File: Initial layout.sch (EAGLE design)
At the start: 50 parts, among them U2 TPS54540DDARQ1

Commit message: Finished Schematic
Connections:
- new net SPARE_1: U$1.P12, U$2.33/A14
- new net SPARE_2: U$1.P11, U$2.34/A15
- new net SPARE_3: U$1.P8, U$2.35/A16
- new net SPARE_4: U$1.P7, U$2.36/A17
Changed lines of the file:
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@@
 <label x="205.74" y="-414.02" size="1.778" layer="95"/>
 <pinref part="U$2" gate="G$1" pin="13/SCK"/>
-<wire x1="274.32" y1="-256.54" x2="287.02" y2="-256.54" width="0.1524" layer="91"/>
-<wire x1="287.02" y1="-256.54" x2="287.02" y2="-314.96" width="0.1524" layer="91"/>
-<wire x1="287.02" y1="-314.96" x2="187.96" y2="-314.96" width="0.1524" layer="91"/>
+<wire x1="274.32" y1="-256.54" x2="299.72" y2="-256.54" width="0.1524" layer="91"/>
+<wire x1="299.72" y1="-256.54" x2="299.72" y2="-314.96" width="0.1524" layer="91"/>
+<wire x1="299.72" y1="-314.96" x2="187.96" y2="-314.96" width="0.1524" layer="91"/>
 <wire x1="187.96" y1="-314.96" x2="187.96" y2="-414.02" width="0.1524" layer="91"/>
 </segment>
@@
 </segment>
 </net>
+<net name="SPARE_1" class="0">
+<segment>
+<pinref part="U$2" gate="G$1" pin="33/A14"/>
+<wire x1="274.32" y1="-281.94" x2="292.1" y2="-281.94" width="0.1524" layer="91"/>
+<label x="287.02" y="-281.94" size="1.778" layer="95"/>
+</segment>
+<segment>
+<pinref part="U$1" gate="G$1" pin="P12"/>
+<wire x1="391.16" y1="-248.92" x2="403.86" y2="-248.92" width="0.1524" layer="91"/>
+<label x="398.78" y="-248.92" size="1.778" layer="95"/>
+</segment>
+</net>
+<net name="SPARE_2" class="0">
+<segment>
+<pinref part="U$2" gate="G$1" pin="34/A15"/>
+<wire x1="274.32" y1="-279.4" x2="292.1" y2="-279.4" width="0.1524" layer="91"/>
+<label x="287.02" y="-279.4" size="1.778" layer="95"/>
+</segment>
+<segment>
+<pinref part="U$1" gate="G$1" pin="P11"/>
+<wire x1="391.16" y1="-246.38" x2="403.86" y2="-246.38" width="0.1524" layer="91"/>
+<label x="398.78" y="-246.38" size="1.778" layer="95"/>
+</segment>
+</net>
+<net name="SPARE_3" class="0">
+<segment>
+<pinref part="U$2" gate="G$1" pin="35/A16"/>
+<wire x1="274.32" y1="-276.86" x2="292.1" y2="-276.86" width="0.1524" layer="91"/>
+<label x="287.02" y="-276.86" size="1.778" layer="95"/>
+</segment>
+<segment>
+<pinref part="U$1" gate="G$1" pin="P8"/>
+<wire x1="391.16" y1="-236.22" x2="403.86" y2="-236.22" width="0.1524" layer="91"/>
+<label x="398.78" y="-236.22" size="1.778" layer="95"/>
+</segment>
+</net>
+<net name="SPARE_4" class="0">
+<segment>
+<pinref part="U$2" gate="G$1" pin="36/A17"/>
+<wire x1="274.32" y1="-274.32" x2="292.1" y2="-274.32" width="0.1524" layer="91"/>
+<label x="287.02" y="-274.32" size="1.778" layer="95"/>
+</segment>
+<segment>
+<pinref part="U$1" gate="G$1" pin="P7"/>
+<wire x1="391.16" y1="-233.68" x2="403.86" y2="-233.68" width="0.1524" layer="91"/>
+<label x="398.78" y="-233.68" size="1.778" layer="95"/>
+</segment>
+</net>

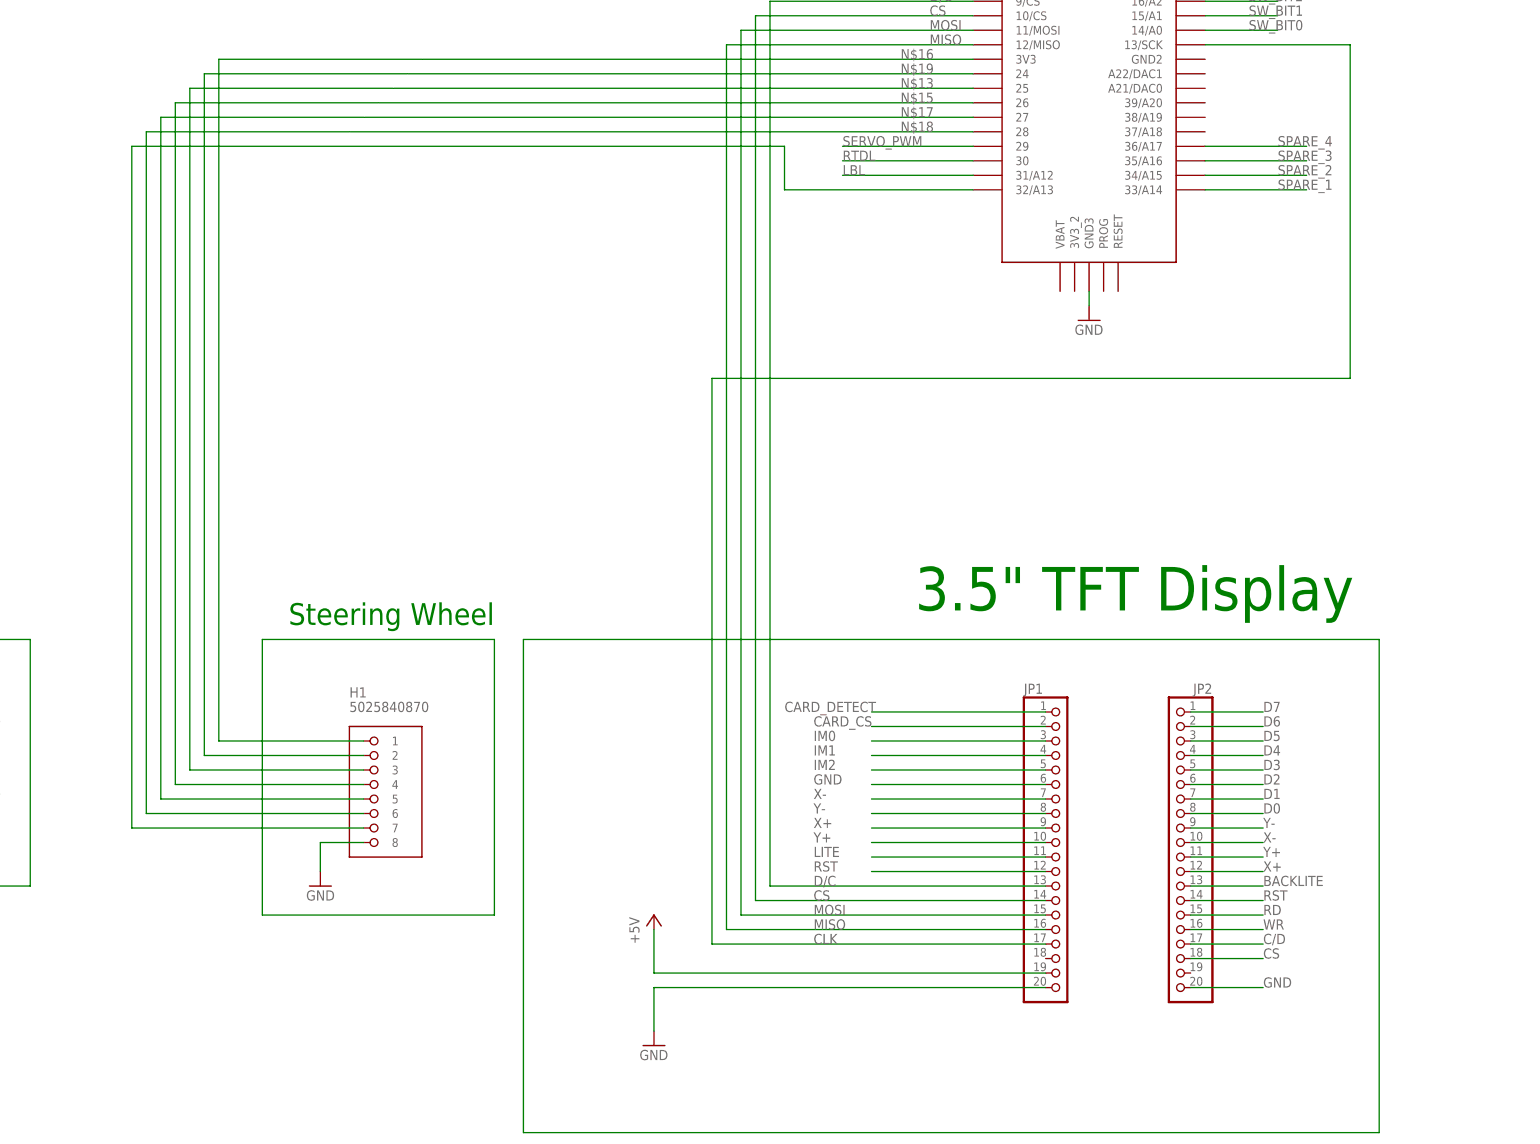
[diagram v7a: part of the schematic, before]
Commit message: Added 4 pin clickmate for rj45
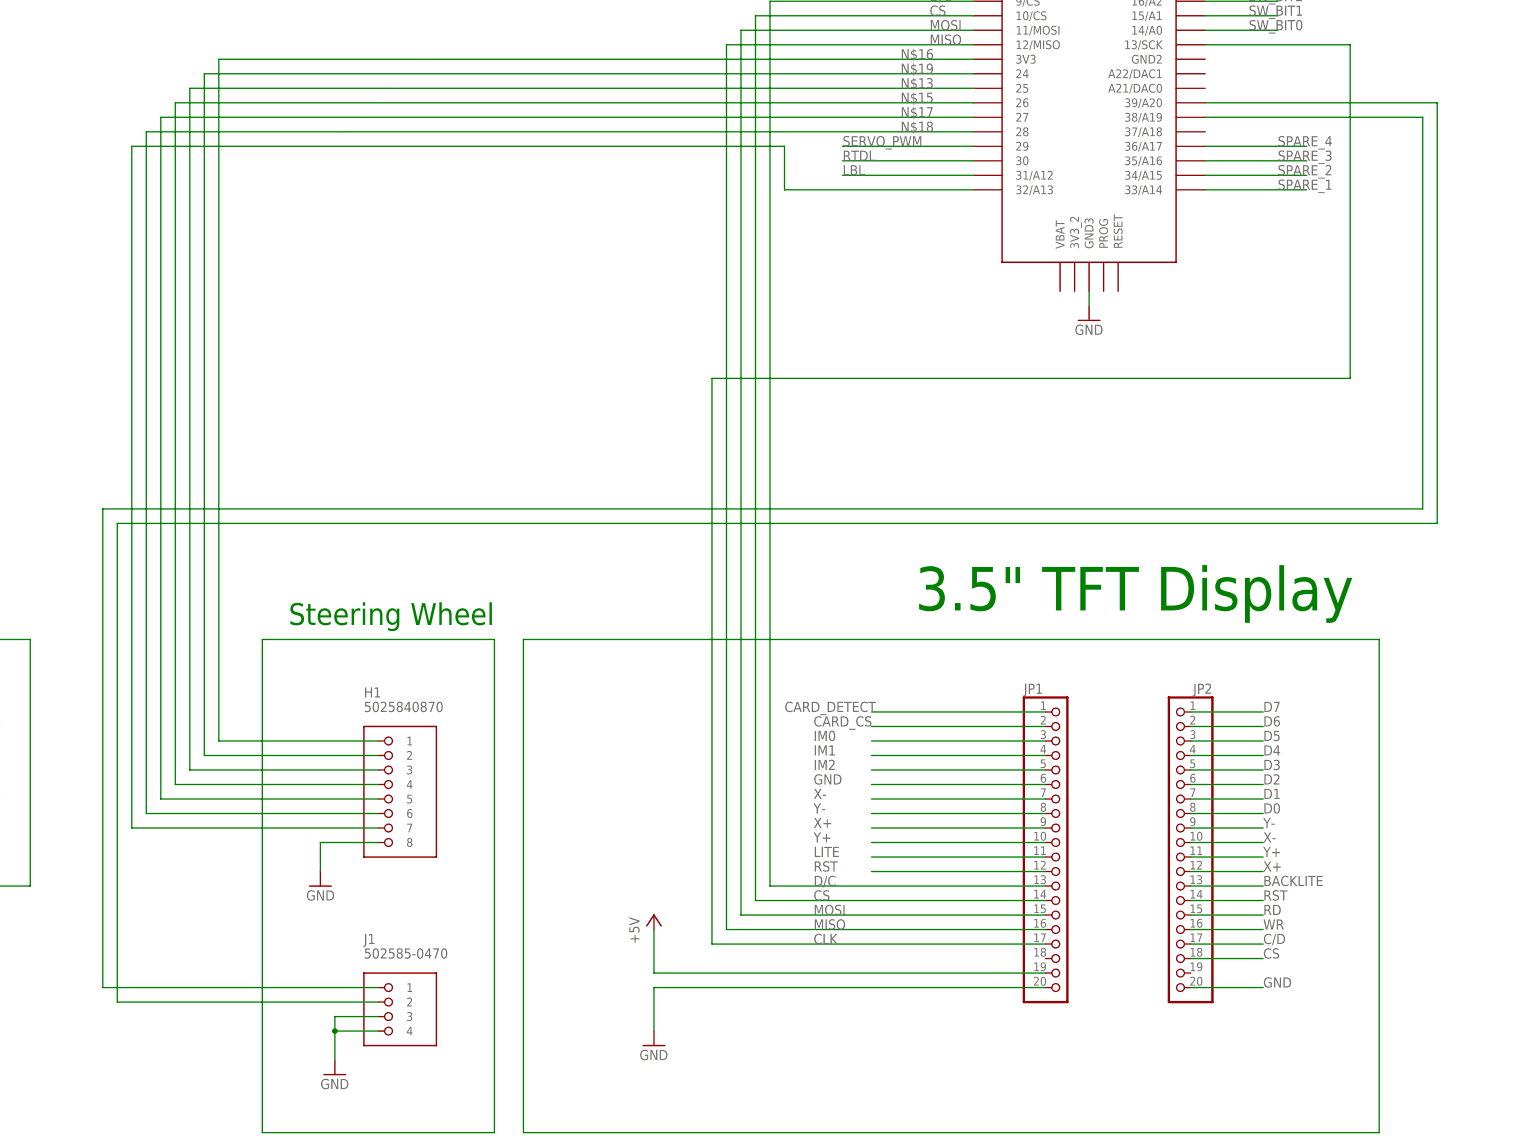
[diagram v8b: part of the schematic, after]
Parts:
- added J1: 502585-0470, FormE:MOLEX_CLICKMATE-4-R/A
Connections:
- new net N$34: J1.1, U$2.38/A19
- new net N$35: J1.2, U$2.39/A20
- net GND: now also J1.3, J1.4
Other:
- moved on the sheet: H1
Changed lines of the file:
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@@
 <layers>
 <layer number="1" name="Top" color="4" fill="1" visible="no" active="no"/>
+<layer number="2" name="GND" color="11" fill="1" visible="no" active="no"/>
+<layer number="3" name="Route3" color="4" fill="3" visible="no" active="no"/>
+<layer number="4" name="Route4" color="1" fill="4" visible="no" active="no"/>
+<layer number="5" name="Route5" color="4" fill="4" visible="no" active="no"/>
+<layer number="6" name="Route6" color="1" fill="8" visible="no" active="no"/>
+<layer number="7" name="Route7" color="4" fill="8" visible="no" active="no"/>
+<layer number="8" name="Route8" color="1" fill="2" visible="no" active="no"/>
+<layer number="9" name="Route9" color="4" fill="2" visible="no" active="no"/>
+<layer number="10" name="Route10" color="1" fill="7" visible="no" active="no"/>
+<layer number="11" name="Route11" color="4" fill="7" visible="no" active="no"/>
+<layer number="12" name="Route12" color="1" fill="5" visible="no" active="no"/>
+<layer number="13" name="Route13" color="4" fill="5" visible="no" active="no"/>
+<layer number="14" name="Route14" color="1" fill="6" visible="no" active="no"/>
+<layer number="15" name="SUPPLY" color="13" fill="1" visible="no" active="no"/>
 <layer number="16" name="Bottom" color="1" fill="1" visible="no" active="no"/>
 <layer number="17" name="Pads" color="2" fill="1" visible="no" active="no"/>
@@
 <part name="GND27" library="supply1" deviceset="GND" device=""/>
 <part name="P+6" library="supply1" deviceset="+5V" device=""/>
+<part name="J1" library="FormE" deviceset="MOLEX_CLICKMATE-4-R/A" device="" value="502585-0470"/>
+<part name="GND23" library="supply1" deviceset="GND" device=""/>
 </parts>
 <sheets>
@@
 <instance part="GND22" gate="1" x="254" y="-304.8"/>
 <instance part="P+7" gate="1" x="431.8" y="-208.28"/>
-<instance part="H1" gate="G$1" x="127" y="-386.08"/>
+<instance part="H1" gate="G$1" x="129.54" y="-386.08"/>
 <instance part="GND24" gate="1" x="119.38" y="-403.86" rot="MR0"/>
 <instance part="U3" gate="G$1" x="30.48" y="-378.46"/>
@@
 <instance part="GND27" gate="1" x="35.56" y="-391.16" rot="R270"/>
 <instance part="P+6" gate="1" x="276.86" y="-198.12"/>
+<instance part="J1" gate="G$1" x="132.08" y="-426.72"/>
+<instance part="GND23" gate="1" x="121.92" y="-436.88"/>
 </instances>
 <busses>
@@
 <segment>
 <pinref part="H1" gate="G$1" pin="8"/>
-<wire x1="127" y1="-396.24" x2="119.38" y2="-396.24" width="0.1524" layer="91"/>
+<wire x1="129.54" y1="-396.24" x2="119.38" y2="-396.24" width="0.1524" layer="91"/>
 <wire x1="119.38" y1="-396.24" x2="119.38" y2="-401.32" width="0.1524" layer="91"/>
 <pinref part="GND24" gate="1" pin="GND"/>
@@
 <wire x1="391.16" y1="-231.14" x2="401.32" y2="-231.14" width="0.1524" layer="91"/>
 <label x="396.24" y="-231.14" size="1.778" layer="95"/>
+</segment>
+<segment>
+<pinref part="J1" gate="G$1" pin="3"/>
+<wire x1="129.54" y1="-426.72" x2="121.92" y2="-426.72" width="0.1524" layer="91"/>
+<pinref part="J1" gate="G$1" pin="4"/>
+<wire x1="121.92" y1="-426.72" x2="121.92" y2="-429.26" width="0.1524" layer="91"/>
+<wire x1="121.92" y1="-429.26" x2="129.54" y2="-429.26" width="0.1524" layer="91"/>
+<wire x1="121.92" y1="-429.26" x2="121.92" y2="-434.34" width="0.1524" layer="91"/>
+<junction x="121.92" y="-429.26"/>
+<pinref part="GND23" gate="1" pin="GND"/>
 </segment>
 </net>
@@
 <pinref part="H1" gate="G$1" pin="7"/>
 <wire x1="86.36" y1="-274.32" x2="200.66" y2="-274.32" width="0.1524" layer="91"/>
-<wire x1="127" y1="-393.7" x2="86.36" y2="-393.7" width="0.1524" layer="91"/>
+<wire x1="129.54" y1="-393.7" x2="86.36" y2="-393.7" width="0.1524" layer="91"/>
 <wire x1="86.36" y1="-393.7" x2="86.36" y2="-274.32" width="0.1524" layer="91"/>
 <pinref part="U$2" gate="G$1" pin="32/A13"/>
@@
 <net name="N$9" class="0">
 <segment>
-<wire x1="149.86" y1="-360.68" x2="149.86" y2="-408.94" width="0.1524" layer="91"/>
-<wire x1="149.86" y1="-408.94" x2="109.22" y2="-408.94" width="0.1524" layer="91"/>
-<wire x1="109.22" y1="-408.94" x2="109.22" y2="-360.68" width="0.1524" layer="91"/>
+<wire x1="149.86" y1="-360.68" x2="149.86" y2="-447.04" width="0.1524" layer="91"/>
+<wire x1="149.86" y1="-447.04" x2="109.22" y2="-447.04" width="0.1524" layer="91"/>
+<wire x1="109.22" y1="-447.04" x2="109.22" y2="-360.68" width="0.1524" layer="91"/>
 <wire x1="109.22" y1="-360.68" x2="149.86" y2="-360.68" width="0.1524" layer="91"/>
 </segment>
@@
 <segment>
 <pinref part="H1" gate="G$1" pin="1"/>
-<wire x1="127" y1="-378.46" x2="101.6" y2="-378.46" width="0.1524" layer="91"/>
+<wire x1="129.54" y1="-378.46" x2="101.6" y2="-378.46" width="0.1524" layer="91"/>
 <wire x1="101.6" y1="-378.46" x2="101.6" y2="-259.08" width="0.1524" layer="91"/>
 <wire x1="101.6" y1="-259.08" x2="137.16" y2="-259.08" width="0.1524" layer="91"/>
@@
 <segment>
 <pinref part="H1" gate="G$1" pin="2"/>
-<wire x1="127" y1="-381" x2="99.06" y2="-381" width="0.1524" layer="91"/>
+<wire x1="129.54" y1="-381" x2="99.06" y2="-381" width="0.1524" layer="91"/>
 <wire x1="99.06" y1="-381" x2="99.06" y2="-261.62" width="0.1524" layer="91"/>
 <wire x1="99.06" y1="-261.62" x2="134.62" y2="-261.62" width="0.1524" layer="91"/>
@@
 <segment>
 <pinref part="H1" gate="G$1" pin="3"/>
-<wire x1="127" y1="-383.54" x2="96.52" y2="-383.54" width="0.1524" layer="91"/>
+<wire x1="129.54" y1="-383.54" x2="96.52" y2="-383.54" width="0.1524" layer="91"/>
 <wire x1="96.52" y1="-383.54" x2="96.52" y2="-264.16" width="0.1524" layer="91"/>
 <wire x1="96.52" y1="-264.16" x2="132.08" y2="-264.16" width="0.1524" layer="91"/>
@@
 <segment>
 <pinref part="H1" gate="G$1" pin="4"/>
-<wire x1="127" y1="-386.08" x2="93.98" y2="-386.08" width="0.1524" layer="91"/>
+<wire x1="129.54" y1="-386.08" x2="93.98" y2="-386.08" width="0.1524" layer="91"/>
 <wire x1="93.98" y1="-386.08" x2="93.98" y2="-266.7" width="0.1524" layer="91"/>
 <wire x1="93.98" y1="-266.7" x2="129.54" y2="-266.7" width="0.1524" layer="91"/>
@@
 <segment>
 <pinref part="H1" gate="G$1" pin="5"/>
-<wire x1="127" y1="-388.62" x2="91.44" y2="-388.62" width="0.1524" layer="91"/>
+<wire x1="129.54" y1="-388.62" x2="91.44" y2="-388.62" width="0.1524" layer="91"/>
 <wire x1="91.44" y1="-388.62" x2="91.44" y2="-269.24" width="0.1524" layer="91"/>
 <wire x1="91.44" y1="-269.24" x2="127" y2="-269.24" width="0.1524" layer="91"/>
@@
 <segment>
 <pinref part="H1" gate="G$1" pin="6"/>
-<wire x1="127" y1="-391.16" x2="88.9" y2="-391.16" width="0.1524" layer="91"/>
+<wire x1="129.54" y1="-391.16" x2="88.9" y2="-391.16" width="0.1524" layer="91"/>
 <wire x1="88.9" y1="-391.16" x2="88.9" y2="-271.78" width="0.1524" layer="91"/>
 <wire x1="88.9" y1="-271.78" x2="124.46" y2="-271.78" width="0.1524" layer="91"/>
@@
 </segment>
 </net>
+<net name="N$34" class="0">
+<segment>
+<pinref part="J1" gate="G$1" pin="1"/>
+<wire x1="129.54" y1="-421.64" x2="81.28" y2="-421.64" width="0.1524" layer="91"/>
+<wire x1="81.28" y1="-421.64" x2="81.28" y2="-337.82" width="0.1524" layer="91"/>
+<wire x1="81.28" y1="-337.82" x2="312.42" y2="-337.82" width="0.1524" layer="91"/>
+<pinref part="U$2" gate="G$1" pin="38/A19"/>
+<wire x1="312.42" y1="-337.82" x2="312.42" y2="-269.24" width="0.1524" layer="91"/>
+<wire x1="312.42" y1="-269.24" x2="274.32" y2="-269.24" width="0.1524" layer="91"/>
+</segment>
+</net>
+<net name="N$35" class="0">
+<segment>
+<pinref part="J1" gate="G$1" pin="2"/>
+<wire x1="129.54" y1="-424.18" x2="83.82" y2="-424.18" width="0.1524" layer="91"/>
+<wire x1="83.82" y1="-424.18" x2="83.82" y2="-340.36" width="0.1524" layer="91"/>
+<wire x1="83.82" y1="-340.36" x2="314.96" y2="-340.36" width="0.1524" layer="91"/>
+<pinref part="U$2" gate="G$1" pin="39/A20"/>
+<wire x1="314.96" y1="-340.36" x2="314.96" y2="-266.7" width="0.1524" layer="91"/>
+<wire x1="314.96" y1="-266.7" x2="274.32" y2="-266.7" width="0.1524" layer="91"/>
+</segment>
+</net>
